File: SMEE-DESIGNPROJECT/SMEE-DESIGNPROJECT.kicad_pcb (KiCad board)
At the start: 2 copper layers, 30 x 120 mm, 15 parts, among them J1 Conn_01x05, U1 TLC555xP

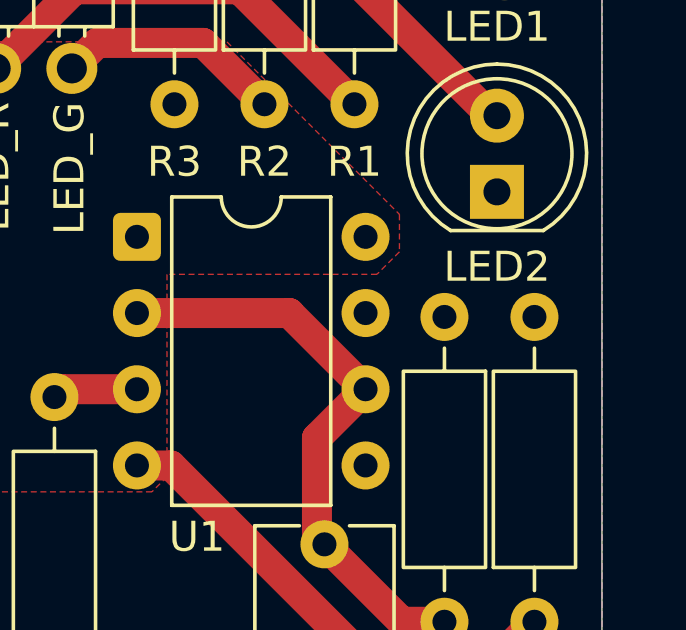
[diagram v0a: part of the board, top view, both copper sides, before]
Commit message: Update PCB routing and zones; add backups
Adjust PCB layout: reroute several segments and update net assignments around U1 and LED footprints, modify zone definitions (net names, priorities, UUIDs, polygons and filled_polygons) and add teardrop/padvia attributes. Add two backup ZIPs under SMEE-DESIGNPROJECT-backups and remove KiCad .lck temporary lock files. These changes tidy up routing and copper zones for the affected nets and include saved backups of the project state.
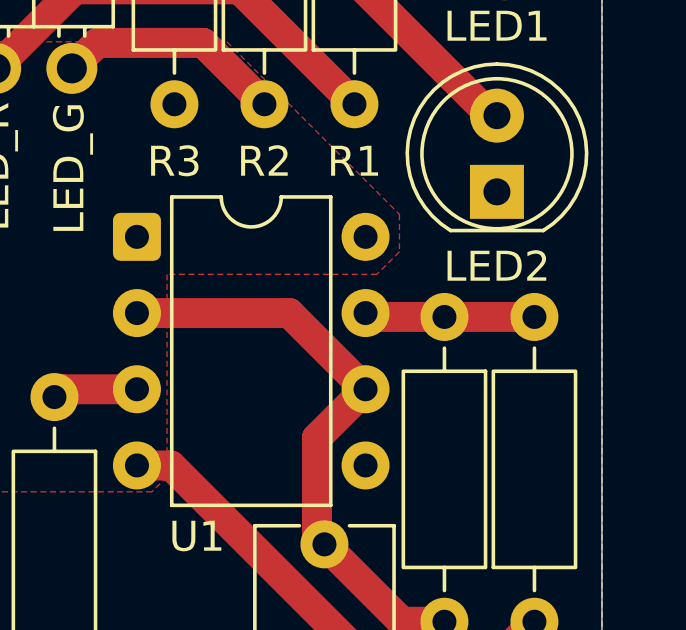
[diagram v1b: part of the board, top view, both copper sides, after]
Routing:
- net Net-(U1-DIS): track 0.00 -> 5.87 mm
